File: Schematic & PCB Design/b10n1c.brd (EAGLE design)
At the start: 14 x 44 mm, 26 parts, among them U1 nRF8001, Y1 16MHz, Y2 FC-255 32.7680K-A3

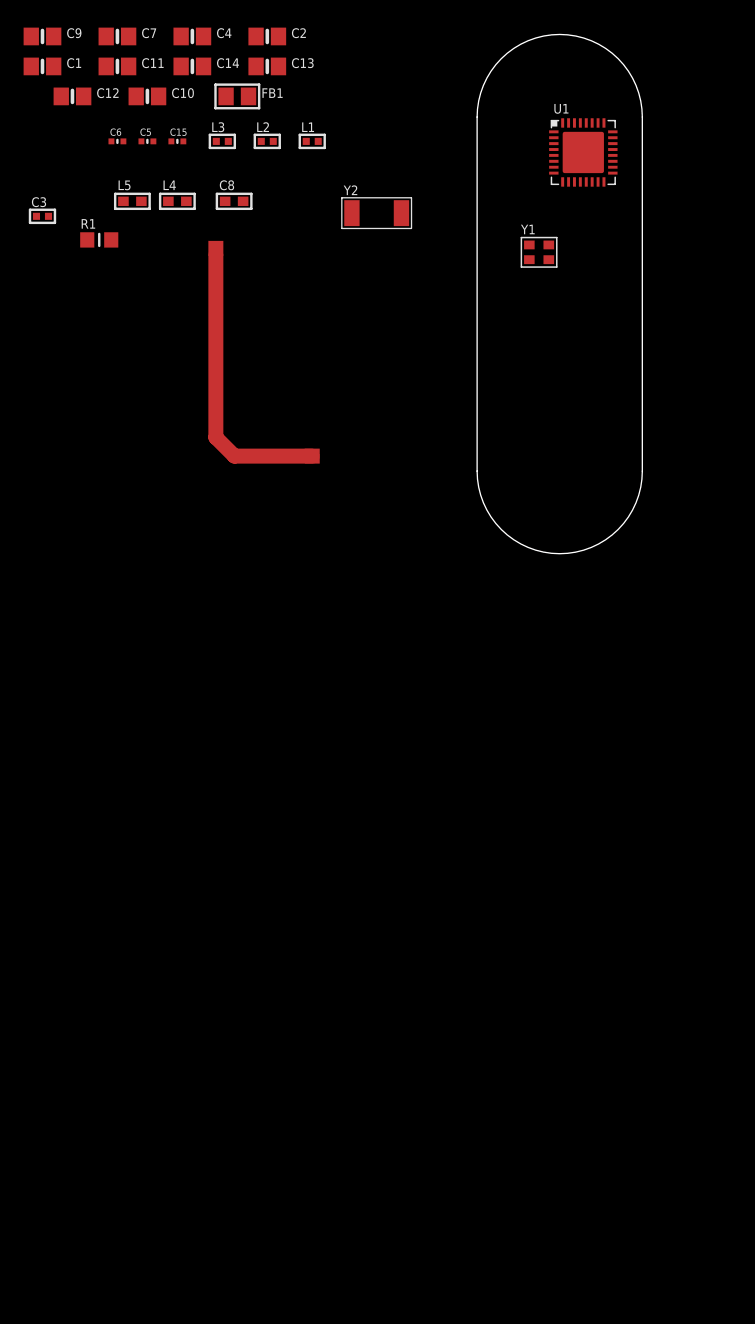
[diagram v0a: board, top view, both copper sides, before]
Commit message: Improvement for NRF8001 circuit
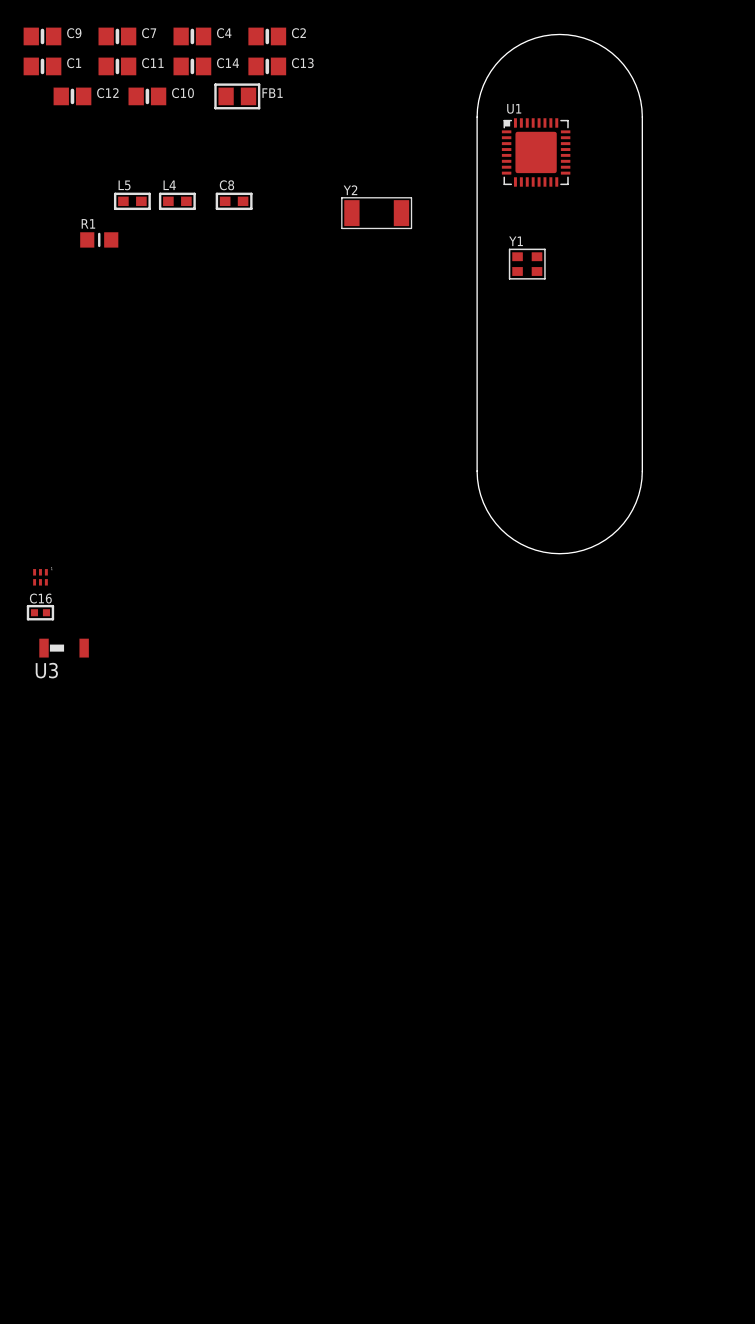
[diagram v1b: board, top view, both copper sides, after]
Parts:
- removed C15: 1.5pF, microbuilder:_0402MP
- removed C3: 2.2nF, microbuilder:_0402
- removed C5: 1.8pF, microbuilder:_0402MP
- removed C6: 1.2pF, microbuilder:_0402MP
- removed L1: 8.2nH, microbuilder:_0402
- removed L2: 5.6nH, microbuilder:_0402
- removed L3: 3.9nH, microbuilder:_0402
- removed U$28: (no value), microbuilder:ANT_PCB_2.4GHZ_NRF8001_1.6MM_1OZ
- added C16: 2.2nF, microbuilder:_0402
- added U2: 2450BM14A0002T, baluns:2450BM14A0002T
- added U3: 2450AT18A100, Johanson_antenna:2450AT18A100
- moved U1 4.00 mm to (5.00, 27.0)
- moved Y1 1.41 mm to (4.25, 17.5)
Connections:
- removed net N$13: C15.2, C5.1, C6.2, U$28.FEED
- removed net N$2: L1.2, L3.1, U1.22
- removed net N$3: L1.1, L2.1, U1.21
- removed net N$4: C3.1, L2.2, U1.20
- removed net N$6: C5.2, L3.2
- new net N$1: C16.1, U1.20, U2.P$5
- new net N$14: U1.21, U2.P$1
- new net N$15: U1.22, U2.P$6
- new net N$16: U2.P$3, U3.P$1
- net GND: now also C16.2, U2.P$2; no longer C15.1, C3.2, C6.1

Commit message: NRF8001 schem+layout completed
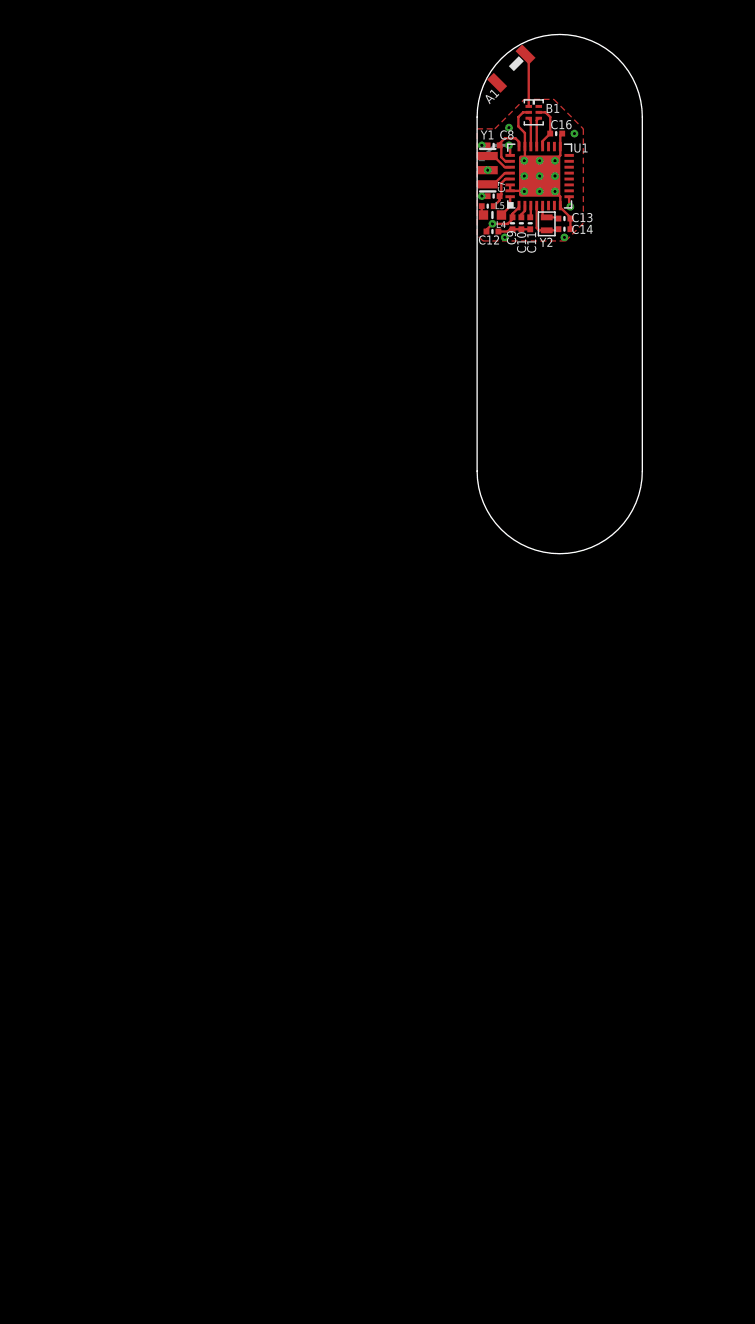
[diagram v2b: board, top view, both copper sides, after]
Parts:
- removed C1, C2: 15pF, microbuilder:0805-NO
- removed C4: 0.1µF, microbuilder:0805-NO
- removed FB1: MMZ1608B121C, microbuilder:0805
- removed U2: 2450BM14A0002T, baluns:2450BM14A0002T
- removed U3: 2450AT18A100, Johanson_antenna:2450AT18A100
- added A1: 2450AT18A100, Johanson_antenna:2450AT18A100
- added B1: 2450BM14A0002T, Johanson_balun:2450BM14A0002T
- C10, C11, C12, C7, C9: device microbuilder:0805-NO -> microbuilder:_0402MP
- C13, C14: value 15pF -> 9pF; device microbuilder:0805-NO -> microbuilder:_0402MP
- C16: device microbuilder:_0402 -> microbuilder:_0402MP
- C8, L5: device microbuilder:_0603 -> microbuilder:_0402MP
- L4: device microbuilder:_0603 -> microbuilder:_0603MP
- R1: device microbuilder:_0805MP -> microbuilder:_0402MP
- Y1: device microbuilder:CRYSTAL_2.5X2 -> SparkFun-FreqCtrl:RESONATOR-SMD
- Y2: value FC-255 32.7680K-A3 -> 32.768; device microbuilder:CRYSTAL_4.9X1.8 -> Crystal-ABS05-32.768KHZ-9-T:CRYSTAL-2PIN
- moved C16 59.6 mm to (6.70, 28.6)
- moved C9 42.9 mm to (3.00, 21.0), turned to 270 degrees
- moved C11 37.4 mm to (4.50, 21.0), turned to 270 degrees
- moved C12 37.4 mm to (1.30, 20.3)
- moved C7 34.6 mm to (1.40, 23.3), turned to 180 degrees
- moved C14 34.4 mm to (7.40, 20.5), turned to 180 degrees
- moved C10 33.5 mm to (3.75, 21.0), turned to 270 degrees
- moved R1 33.0 mm to (0.40, 26.0), flipped to the bottom, turned to 270 degrees
- moved L5 30.1 mm to (0.90, 22.4)
- moved C13 28.3 mm to (7.40, 21.4), turned to 180 degrees
- moved L4 26.7 mm to (1.30, 21.7), turned to 180 degrees
- moved C8 22.5 mm to (1.40, 27.6), turned to 180 degrees
- moved Y2 14.4 mm to (5.90, 20.9), turned to 270 degrees
- moved Y1 8.64 mm to (0.90, 25.5), turned to 270 degrees
- moved U1 2.02 mm to (5.30, 25.0), turned to 90 degrees
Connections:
- removed net AVDD: C4.1, C7.1, C8.1, FB1.2, L5.2, U1.24, U1.26, U1.29
- removed net GND: C1.2, C10.2, C11.2, C12.2, C13.1, C14.1, C16.2, C2.2, C4.2, C7.2, C8.2, C9.2, R1.2, U1.17, U1.18, U1.23, U1.30, U1.31, U1.33, U1.8, U2.P$2
- removed net VDD: C12.1, C9.1, FB1.1, U1.1, U1.9
- new net GND2: B1.2, C10.2, C11.2, C12.2, C13.1, C14.1, C16.2, C7.2, C8.2, C9.2, R1.2, U1.17, U1.18, U1.23, U1.30, U1.31, U1.33, U1.8, Y1.2
- new net N$2: C7.1, L5.2, U1.29
- new net N$3: C8.1, U1.24, U1.26
- new net VCC: C12.1, C9.1, U1.1, U1.9
- net N$1: now also B1.5; no longer U2.P$5
- net N$10: no longer C2.1
- net N$14: now also B1.4; no longer U2.P$1
- net N$15: now also B1.3; no longer U2.P$6
- net N$16: now also A1.P$1, B1.1; no longer U2.P$3, U3.P$1
- net N$9: no longer C1.1
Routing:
- net GND2: track 0.00 -> 25.3 mm, vias 0 -> 16
- net VCC: track 0.00 -> 4.84 mm, vias 0 -> 2
- net N$3: track 0.00 -> 4.66 mm
- net N$16: track 0.00 -> 4.52 mm
- net N$1: track 0.00 -> 3.91 mm
- net N$22: track 0.00 -> 3.87 mm
- net N$12: track 0.00 -> 3.64 mm, vias 0 -> 1
- net N$2: track 0.00 -> 3.11 mm
- net N$15: track 0.00 -> 2.47 mm
- net N$14: track 0.00 -> 2.47 mm
- net N$23: track 0.00 -> 2.38 mm
- net N$9: track 0.00 -> 2.29 mm
- net N$10: track 0.00 -> 2.29 mm
- net N$11: track 0.00 -> 1.86 mm
- net N$8: track 0.00 -> 1.12 mm
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- added copper zone on layer 1, net GND2
- added copper zone on layer 2, net GND2
- added copper zone on layer 15, net VCC

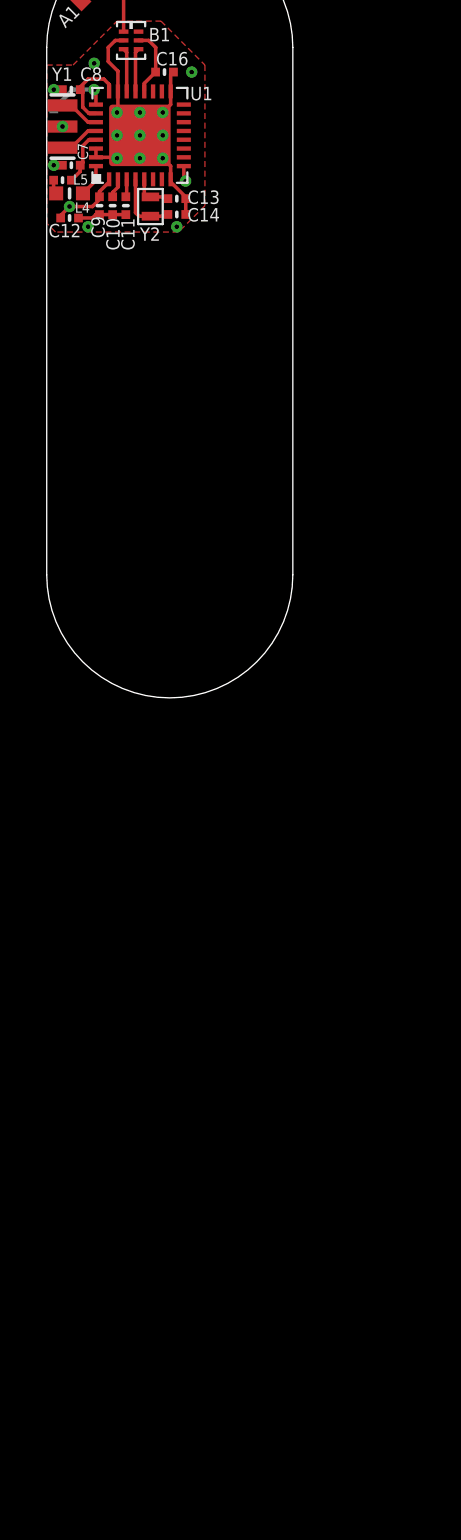
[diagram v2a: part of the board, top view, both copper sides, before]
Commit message: ATMEGA328 & PN532 circuit added to b10n1c schamtic
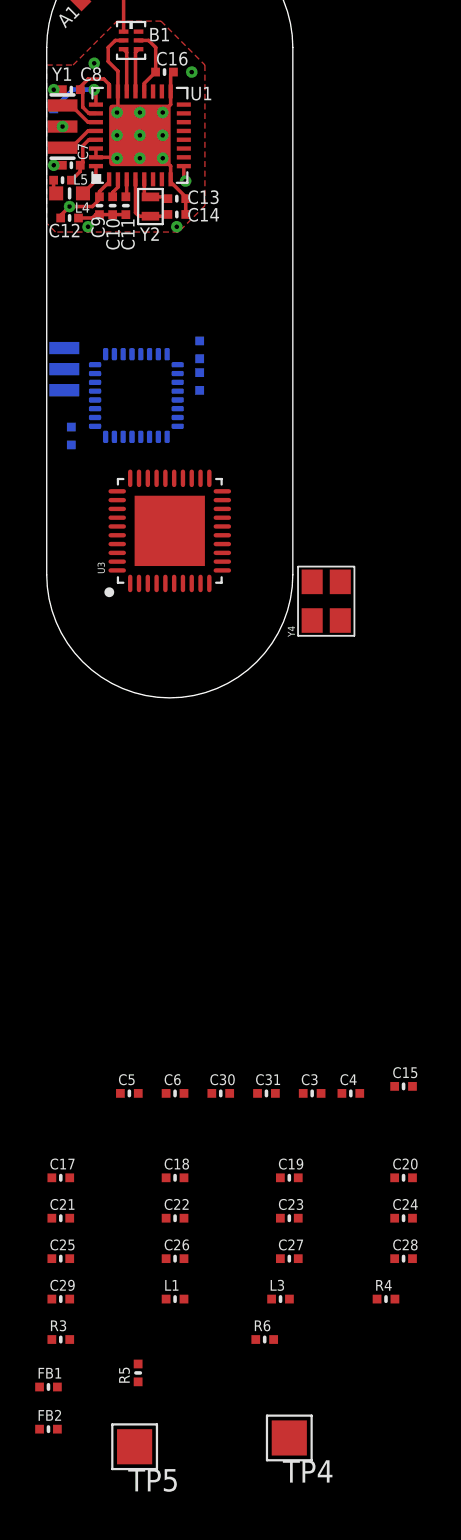
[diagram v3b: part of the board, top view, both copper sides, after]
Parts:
- added C1, C15, C19, C2, C21, C22, C25, C27, C28: 0.1µF, microbuilder:_0402MP
- added C17, C18: 33pF, microbuilder:_0402MP
- added C20: 1000pF, microbuilder:_0402MP
- added C23, C24, C26, C29: 10µF, microbuilder:_0402MP
- added C3, C4: 22pF, microbuilder:_0402MP
- added C30, C31: 220pF, microbuilder:_0402MP
- added C5, C6: 100pF, microbuilder:_0402MP
- added FB1, FB2: (no value), microbuilder:_0402MP
- added L1, L3: 560nH, microbuilder:_0402MP
- added R2: 10K, microbuilder:_0402MP
- added R3: 1.0K, microbuilder:_0402MP
- added R4: 1.69K, microbuilder:_0402MP
- added R5, R6: 1.5, microbuilder:_0402MP
- added TP4: TX2_PRE, microbuilder:TESTPOINT_PAD_2MM
- added TP5: TX1_PRE, microbuilder:TESTPOINT_PAD_2MM
- added U2: ATMEGA328P-MU, Smartprj:MLF32-M1-A
- added U3: PN532, microbuilder:HVQFN40-6X6
- added Y3: 8MHZ, SparkFun-FreqCtrl:RESONATOR-SMD
- added Y4: 27.12MHz, microbuilder:CRYSTAL_3.2X2.5
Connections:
- removed net RDYN: U1.16
- removed net REQN: U1.12
- new net +3V3: C1.1, R2.2, U2.18, U2.4, U2.6
- new net ADC2: U2.25
- new net ADC3: U2.26
- new net ADC6: U2.19
- new net ADC7: U2.22
- new net AREF: C2.1, U2.20
- new net AUX1: U3.12
- new net AUX2: U3.13
- new net GND: C1.2, C15.2, C17.2, C18.2, C19.2, C2.2, C21.2, C22.2, C23.2, C24.2, C25.2, C26.1, C27.2, C28.2, C29.2, C30.2, C31.1, C5.2, C6.1, U2.21, U2.3, U2.5, U3.1, U3.11, U3.18, U3.3, U3.7, U3.TP, Y3.2
- new net IO2: U2.32
- new net IO3: U2.1
- new net IO4: U2.2
- new net IO5: U2.9
- new net IO6: U2.10
- new net IO7: U2.11
- new net IO8: U2.12
- new net IO9: U2.13
- new net IRQ: U3.25
- new net N$13: L3.2, U3.4
- new net N$17: L1.2, U3.6
- new net N$18: C3.2, C30.1, L3.1
- new net N$19: C17.1, U3.14, Y4.1
- new net N$20: C18.1, U3.15, Y4.2
- new net N$21: C19.1, R3.2, U3.9
- new net N$24: C20.2, R3.1, U3.10
- new net N$25: C20.1, R4.1
- new net N$26: C31.2, C4.1, L1.1, R4.2
- new net N$27: R5.1, TP5.P$1
- new net N$28: R6.2, TP4.P$1
- new net N$29: C15.1, C29.1, FB2.2, U3.8
- new net N$30: C24.1, C27.1, FB1.2, U3.5
- new net N$4: U2.7, Y3.3
- new net N$6: U2.8, Y3.1
- new net P31: U3.31
- new net P32: U3.32
- new net P33: U3.33
- new net P34/SIC_CLK: U3.34
- new net P35: U3.19
- new net RDY: U1.16, U2.24
- new net REQ: U1.12, U2.14
- new net RST: U1.19, U2.23
- new net RSTOUT_N: U3.26
- new net RSTPD_N: U3.38
- new net RX: U2.30
- new net SCL: U2.28, U3.27
- new net SDA: U2.27, U3.28
- new net SEL0: U3.16
- new net SEL1: U3.17
- new net SIGIN: U3.36
- new net SIGOUT: U3.35
- new net TX: U2.31
- new net TX1_ANTENNA: C3.1, C5.1, R5.2
- new net TX2_ANTENNA: C4.2, C6.2, R6.1
- new net VDD: C21.1, C22.1, C23.1, C25.1, C26.2, C28.1, FB1.1, FB2.1, U3.23, U3.37, U3.39, U3.40
- net MISO: now also U2.16
- net MOSI: now also U2.15
- net RESET: now also R2.1, U2.29; no longer U1.19
- net SCK: now also U2.17

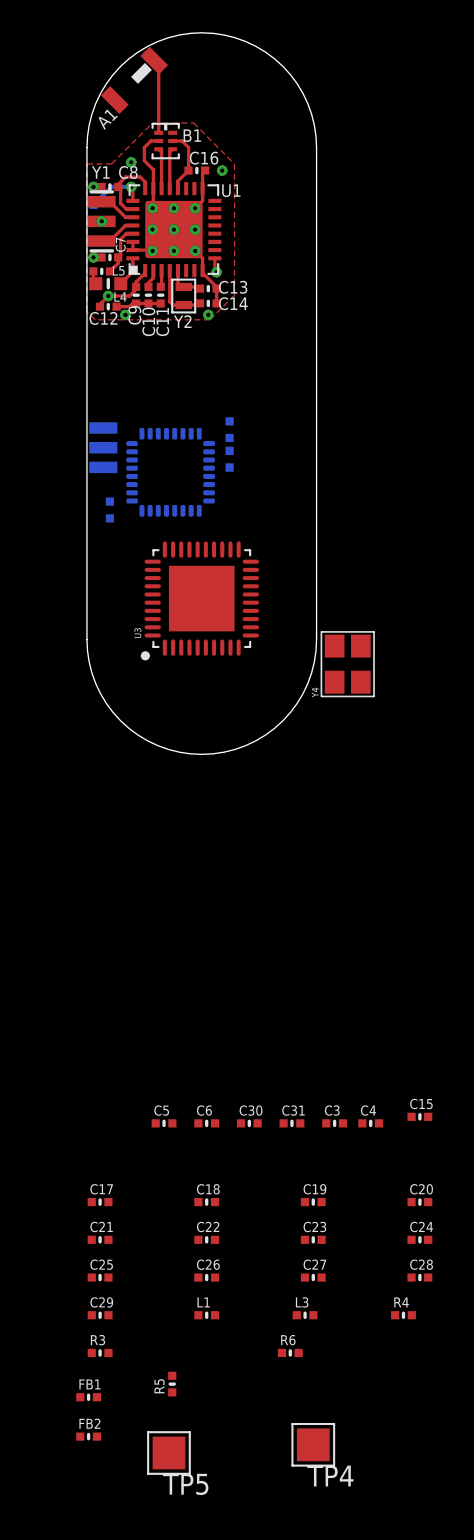
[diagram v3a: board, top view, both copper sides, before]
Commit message: PCB and Schem updated, new Eagle libs
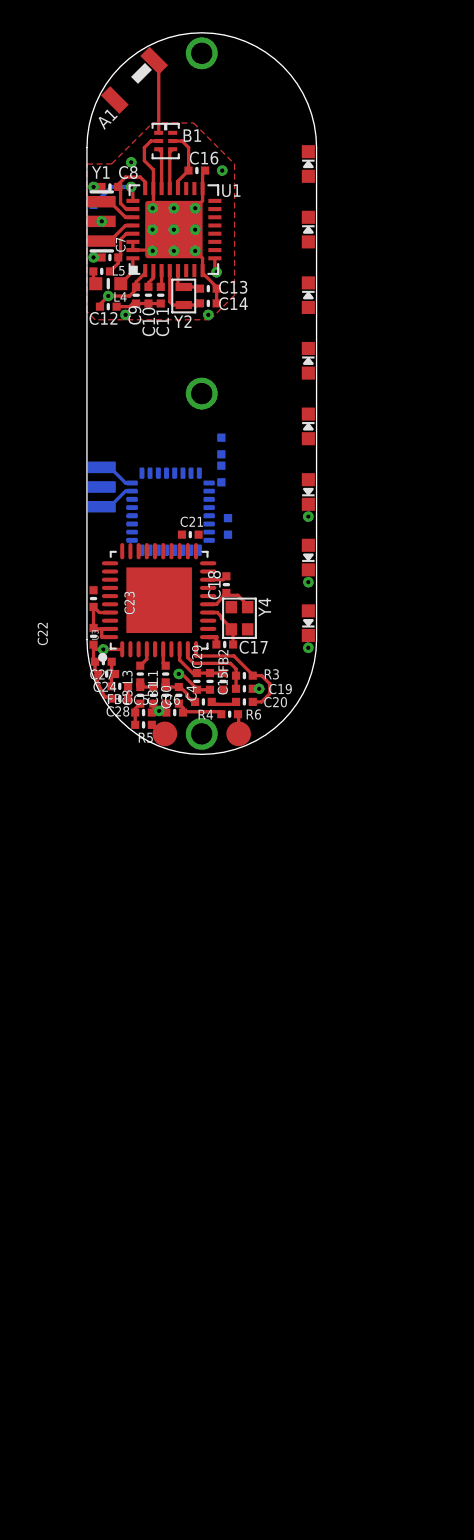
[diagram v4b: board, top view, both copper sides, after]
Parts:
- removed C25: 0.1µF, microbuilder:_0402MP
- removed C26: 10µF, microbuilder:_0402MP
- removed TP4: TX2_PRE, microbuilder:TESTPOINT_PAD_2MM
- removed TP5: TX1_PRE, microbuilder:TESTPOINT_PAD_2MM
- added LED1, LED2, LED3, LED4, LED5, LED6, LED7, LED8: (no value), microbuilder:CHIPLED_0603_NOOUTLINE
- added TP1: TX1_PRE, microbuilder:TESTPOINT_ROUND_1MM
- added TP2: TX2_PRE, microbuilder:TESTPOINT_ROUND_1MM
- added U$3, U$5, U$6: MAKE-UB312-MICRO, pads-for-MAKE-UB312-micro:MAKE-UB312-MICRO
- Y4: device microbuilder:CRYSTAL_3.2X2.5 -> Crystal-Murata-XRCGB27M120F3M00R0:CRYSTAL-MURATA-XRCGB27M120F3M00R0
- moved FB2 46.8 mm to (8.30, -2.55), turned to 90 degrees
- moved FB1 43.4 mm to (2.00, -2.85), turned to 180 degrees
- moved C21 43.4 mm to (6.30, 6.40)
- moved R3 42.2 mm to (9.60, -2.20), turned to 180 degrees
- moved C23 41.3 mm to (0.40, 2.50), turned to 90 degrees
- moved L3 40.4 mm to (3.25, -2.10), turned to 90 degrees
- moved R5 40.2 mm to (3.45, -5.20), turned to 180 degrees
- moved C28 39.8 mm to (2.00, -3.60), turned to 180 degrees
- moved C27 39.7 mm to (1.00, -1.35), turned to 180 degrees
- moved C24 39.4 mm to (1.20, -2.10), turned to 180 degrees
- moved R4 39.3 mm to (7.10, -3.80), turned to 180 degrees
- moved L1 39.2 mm to (4.80, -2.10), turned to 90 degrees
- moved R6 39.1 mm to (8.70, -4.55)
- moved C29 39.1 mm to (6.70, -2.55), turned to 270 degrees
- moved C18 37.7 mm to (8.50, 3.35), turned to 90 degrees
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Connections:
- net GND: now also LED1.C, LED2.C, LED3.C, LED4.C, LED5.C, LED6.C, LED7.C, LED8.C; no longer C25.2, C26.1
- net IO2: now also LED1.A
- net IO3: now also LED2.A
- net IO4: now also LED3.A
- net IO5: now also LED4.A
- net IO6: now also LED5.A
- net IO7: now also LED6.A
- net IO8: now also LED7.A
- net IO9: now also LED8.A
- net N$20: now also Y4.3; no longer Y4.2
- net N$27: now also TP1.P$1; no longer TP5.P$1
- net N$28: now also TP2.P$1; no longer TP4.P$1
- net VDD: no longer C25.1, C26.2
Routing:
- net GND: track 0.00 -> 13.5 mm, vias 0 -> 7
- net N$24: track 0.00 -> 7.49 mm
- net VDD: track 0.00 -> 5.23 mm
- net N$21: track 0.00 -> 4.95 mm
- net N$29: track 0.00 -> 3.64 mm
- net N$20: track 0.00 -> 3.22 mm
- net TX2_ANTENNA: track 0.00 -> 3.19 mm
- net N$19: track 0.00 -> 3.15 mm
- net N$26: track 0.00 -> 2.57 mm
- net N$4: track 0.00 -> 2.24 mm
- net N$6: track 0.00 -> 2.24 mm
- net N$25: track 0.00 -> 2.15 mm
- net N$30: track 0.00 -> 1.67 mm
- net TX1_ANTENNA: track 0.00 -> 1.42 mm
- net N$28: track 0.00 -> 1.25 mm
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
